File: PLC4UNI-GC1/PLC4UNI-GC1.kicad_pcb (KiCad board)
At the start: 4 copper layers, 102.4 x 83.1 mm, 160 parts, among them J1 Conn_02x07_Odd_Even, K1 G5V-1, K2 G5V-1, Q1 NCE60P04R, Q2 ZXMS6004FFQTA, Q3 ZXMS6004FFQTA, Q4 ZXMS6004FFQTA, Q5 ZXMS6004FFQTA, SW1 TS-1088-AR02016, U1 ESP32-S3-WROOM-1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

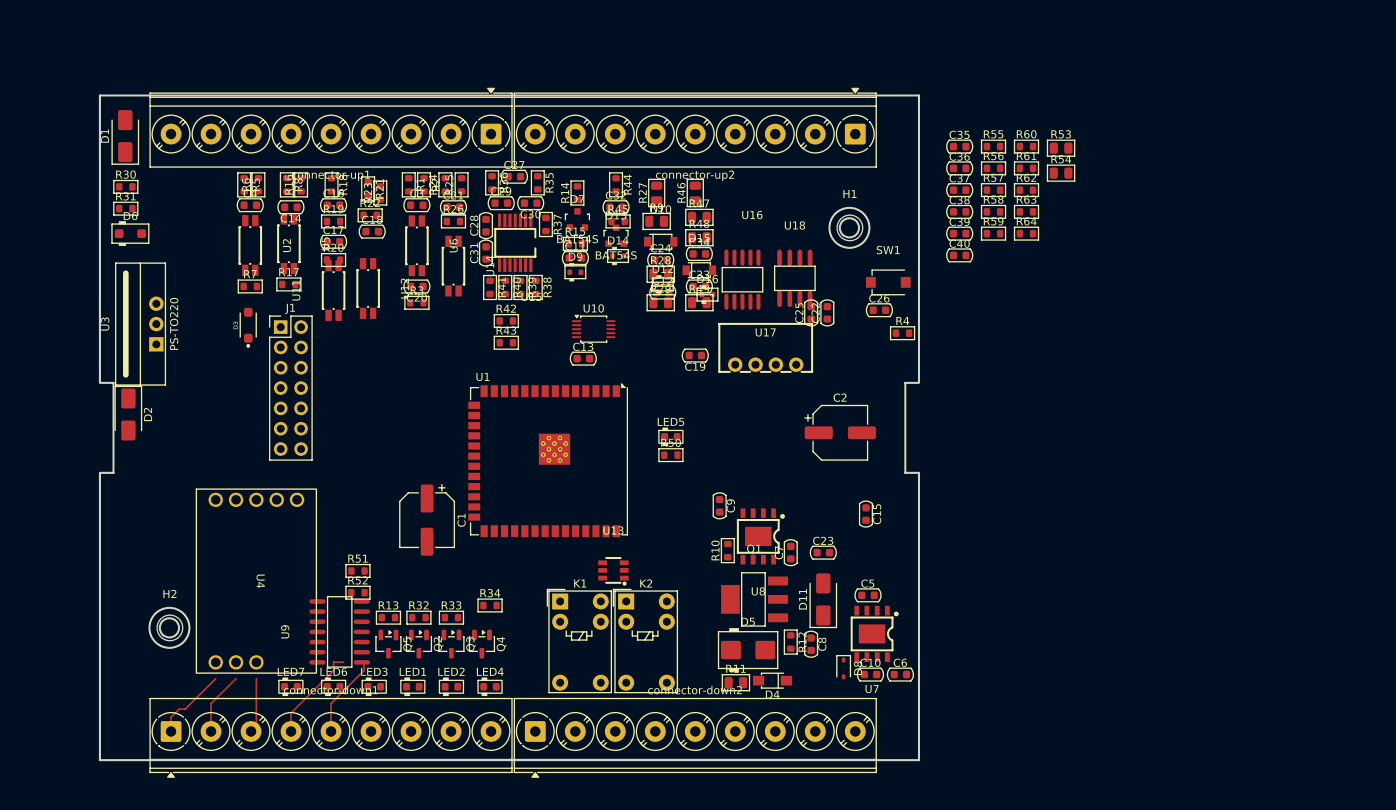
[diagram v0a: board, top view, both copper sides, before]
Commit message: Colocadas el 80% de las piezas
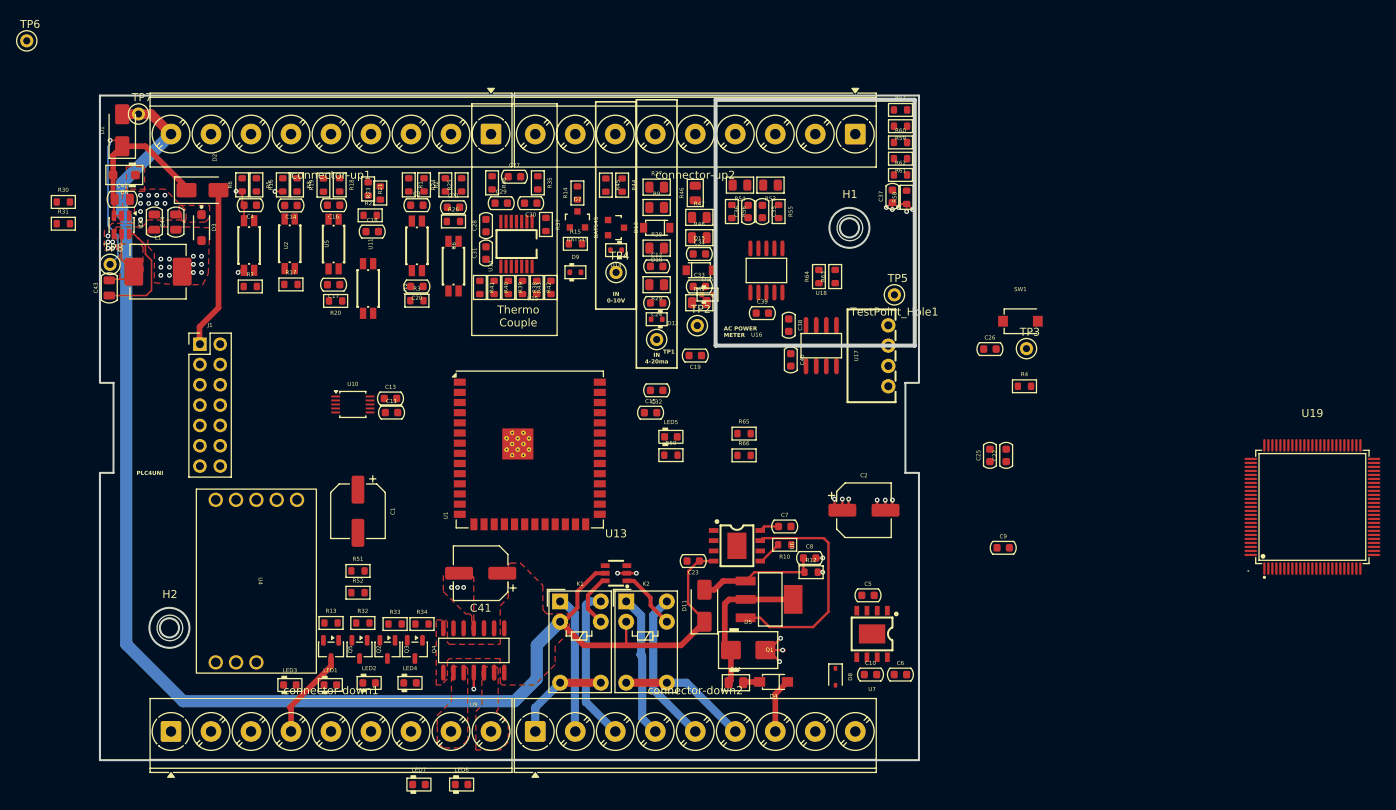
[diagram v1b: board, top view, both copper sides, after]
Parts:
- added C41: 47UF, Capacitor_SMD:CP_Elec_6.3x7.7, F.Cu at (134.6, 120.4)
- added C42: 10uF, Capacitor_SMD_AKL:C_0805_2012Metric, F.Cu at (89.8, 73.7)
- added C43: 100NF, Capacitor_SMD_AKL:C_0805_2012Metric, F.Cu at (88.2, 84.8)
- added C44: 22uF, Capacitor_SMD_AKL:C_0805_2012Metric, F.Cu at (96.5, 76.5)
- added C45: 22uF, Capacitor_SMD_AKL:C_0805_2012Metric, F.Cu at (93.8, 76.5)
- added L1: 10uH, Inductor_SMD:L_APV_APH0630, F.Cu at (94.3, 82.7)
- added R65: 4.7K, Resistor_SMD_AKL:R_0603_1608Metric, F.Cu at (167.5, 103.0)
- added R66: 4.7K, Resistor_SMD_AKL:R_0603_1608Metric, F.Cu at (167.5, 105.7)
- added TP1: TestPoint_Hole1, 4ms_TestPoint:TestPoint_WireHole, F.Cu at (156.6, 91.2)
- added TP2: TestPoint_Hole1, 4ms_TestPoint:TestPoint_WireHole, F.Cu at (161.7, 89.5)
- added TP3: TestPoint_Hole1, 4ms_TestPoint:TestPoint_WireHole, F.Cu at (202.8, 92.4)
- added TP4: TestPoint_Hole1, 4ms_TestPoint:TestPoint_WireHole, F.Cu at (151.5, 82.8)
- added TP5: TestPoint_Hole1, 4ms_TestPoint:TestPoint_WireHole, F.Cu at (186.3, 85.6)
- added TP6: TestPoint_Hole1, 4ms_TestPoint:TestPoint_WireHole, F.Cu at (77.9, 53.9)
- added TP7: TestPoint_Hole1, 4ms_TestPoint:TestPoint_WireHole, F.Cu at (91.8, 63.0)
- added TP8: TestPoint_Hole1, 4ms_TestPoint:TestPoint_WireHole, F.Cu at (88.3, 81.8)
- added U19: LCMXO256C-3TN100C, EasyEDA:TQFP-100_L14.0-W14.0-P0.50-LS16.0-BL, F.Cu at (238.6, 112.1)
- R14, R44: value 3.3K -> 2.2K
- R15, R45: value 2.2K -> 1.05K
- R17, R20, R23, R26, R3, R7: value 10K -> 22K
- U3: value PS-TO220 -> AP63203WU; footprint MG_footprints:PS-TO-220-3_Vertical -> Package_TO_SOT_SMD:TSOT-23-6
- moved R54 40.2 mm to (167.0, 71.9), turned to 180 degrees
- moved R53 36.6 mm to (170.8, 71.9), turned to 180 degrees
- moved C9 35.8 mm to (199.9, 117.3), turned to 0 degrees
- moved R56 33.2 mm to (166.0, 75.2), turned to -90 degrees
- moved U10 31.5 mm to (118.6, 99.3)
- moved C11 30.0 mm to (123.4, 100.3)
- moved C15 29.8 mm to (155.8, 100.4), turned to 0 degrees
- moved D2 29.5 mm to (99.8, 72.5), turned to 0 degrees
- moved C22 28.6 mm to (200.3, 105.7)
- moved C25 28.6 mm to (198.2, 105.7)
- moved R55 28.1 mm to (171.8, 75.2), turned to -90 degrees
- moved C36 27.0 mm to (168.0, 75.2), turned to 90 degrees
- moved C39 26.6 mm to (169.8, 87.9)
- moved R64 26.5 mm to (176.9, 83.3), turned to 90 degrees
- moved C35 26.0 mm to (169.8, 75.2), turned to -90 degrees
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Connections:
- D1 pad 1: Net-(D1-K) -> /PowerSupply/vdc_in
- D2 pad 1: Net-(D1-K) -> /PowerSupply/vdc_in
- D6 pad 2: +24V -> /PowerSupply/vdc_in
- U3 pad 1: Net-(D1-K) -> +3.3V
- U3 pad 2: GND -> /PowerSupply/vdc_in
- U3 pad 3: +3.3V -> /PowerSupply/vdc_in
- connector-down1 pad 4: /control/CON_OUT_PNP1 -> /control/CON_OUT_NPN1
- connector-down1 pad 5: /control/CON_OUT_PNP2 -> /control/CON_OUT_NPN2
- connector-down1 pad 6: /control/CON_OUT_NPN1 -> /control/CON_OUT_NPN3
- connector-down1 pad 7: /control/CON_OUT_NPN2 -> /control/CON_OUT_NPN4
- connector-down1 pad 8: /control/CON_OUT_NPN3 -> /control/CON_OUT_PNP1
- connector-down1 pad 9: /control/CON_OUT_NPN4 -> /control/CON_OUT_PNP2
- connector-down2 pad 4: /control/CON_OUT_RLY2_COM -> /control/CON_OUT_RLY2_NC
- connector-down2 pad 5: /control/CON_OUT_RLY2_NC -> /control/CON_OUT_RLY2_NO
- connector-down2 pad 6: /control/CON_OUT_RLY2_NO -> /control/CON_OUT_RLY2_COM
- connector-up2 pad 1: /control/CON-IN_CT_P -> /control/CON-IN_VAC_P
- connector-up2 pad 2: /control/CON-IN_CT_N -> Earth
- connector-up2 pad 3: /control/CON-IN_VAC_P -> /control/CON-IN_CT_P
- connector-up2 pad 4: /control/CON-IN_VAC_N -> /control/CON-IN_CT_N
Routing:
- net +24V: track 0.00 -> 202.6 mm, vias 0 -> 2
- net /PowerSupply/vdc_in: track 0.00 -> 39.1 mm, vias 0 -> 1
- net Net-(U8-IOUT): track 0.00 -> 29.1 mm
- net +5V: track 0.00 -> 20.5 mm
- net /control/CON_OUT_RLY1_NO: track 0.00 -> 19.4 mm
- net Net-(D5-K): track 0.00 -> 19.3 mm
- net /control/CON_OUT_RLY2_NO: track 0.00 -> 19.1 mm
- net GND: track 0.00 -> 19.1 mm, vias 0 -> 29
- net /control/CON_OUT_RLY2_NC: track 0.00 -> 17.9 mm
- net /control/CON_OUT_RLY1_NC: track 0.00 -> 17.2 mm
- net /control/CON_OUT_RLY2_COM: track 0.00 -> 16.2 mm
- net Net-(D11-A2): track 0.00 -> 15.3 mm
- net Net-(U3-BST): track 0.00 -> 14.1 mm
- net /control/CON_OUT_RLY1_COM: track 0.00 -> 12.5 mm
- net /control/CON_OUT_PNP1: track 12.1 -> 0.00 mm
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- added copper zone on F.Cu, net +24V
- added copper zone on F.Cu, net +3.3V
- added copper zone on In2.Cu, net +3.3V
- added copper zone on F.Cu, net /PowerSupply/sw
- added copper zone on F.Cu, net /control/CON_OUT_PNP1
- added copper zone on F.Cu, net /control/CON_OUT_PNP2
- added copper zone on In1.Cu, net Earth
- added copper zone on F.Cu, net GND
- added copper zone on In1.Cu, net GND
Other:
- outline, holes or cut-outs redrawn
- board text added: "AC POWER METER"
- board text added: "IN 0-10V"
- board text added: "IN 4-20ma"
- board text added: "PLC4UNI"
- board text added: "Thermo Couple"

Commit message: Avances en colocacion de piezas y verificacion de componentes
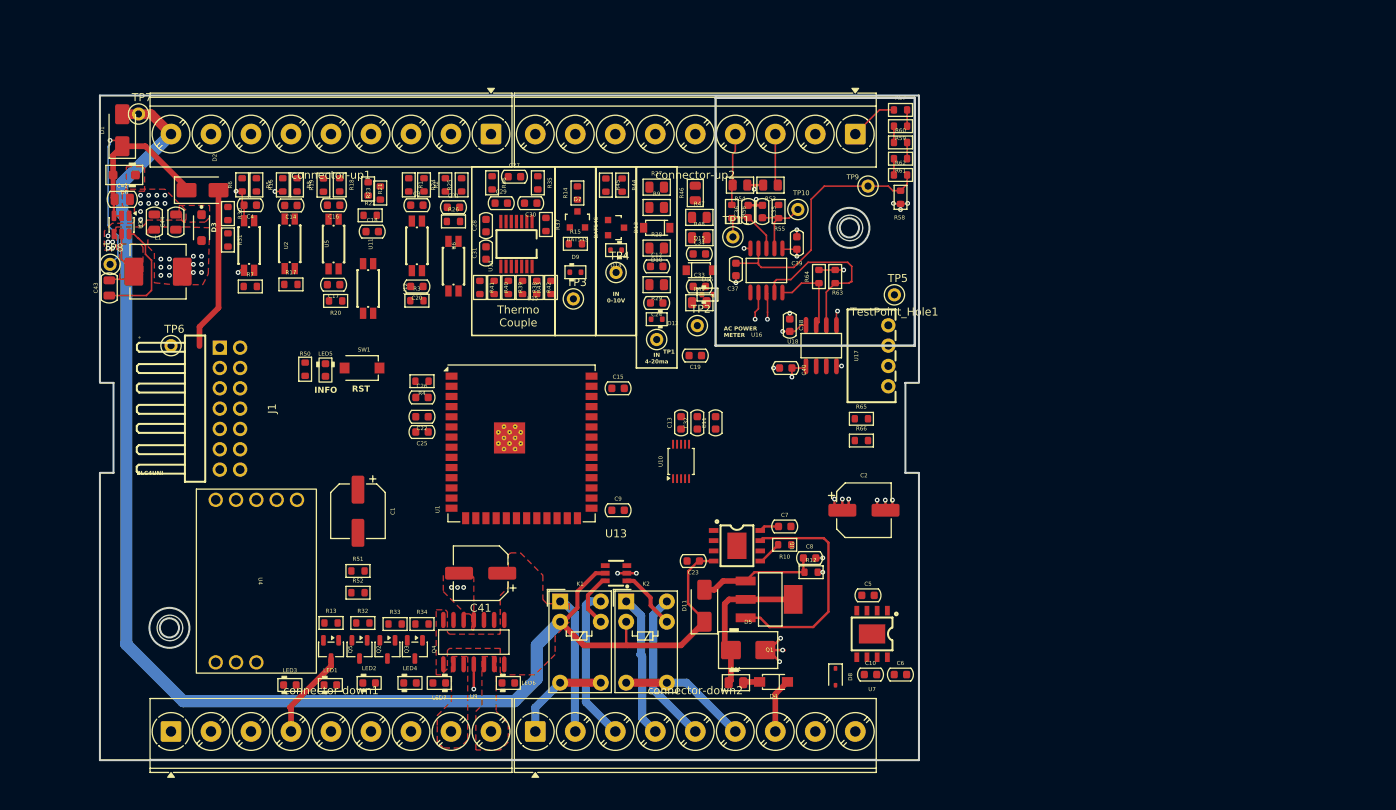
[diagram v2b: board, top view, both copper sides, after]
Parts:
- removed U19: LCMXO256C-3TN100C, EasyEDA:TQFP-100_L14.0-W14.0-P0.50-LS16.0-BL
- added TP10: TestPoint_Hole1, 4ms_TestPoint:TestPoint_WireHole, F.Cu at (174.2, 75.0)
- added TP11: TestPoint_Hole1, 4ms_TestPoint:TestPoint_WireHole, F.Cu at (166.1, 78.4)
- added TP9: TestPoint_Hole1, 4ms_TestPoint:TestPoint_WireHole, F.Cu at (183.0, 72.0)
- J1: value Conn_02x07_Odd_Even -> PZ254R-12-14P; footprint Connector_PinHeader_2.54mm:PinHeader_2x07_P2.54mm_Vertical -> EasyEDA:HDR-TH_14P-P2.54-H-M-R2-C7-S2.54
- moved SW1 82.5 mm to (119.8, 94.8), turned to 180 degrees
- moved R4 75.3 mm to (127.3, 96.4), turned to 180 degrees
- moved C22 73.2 mm to (127.3, 100.9), turned to 180 degrees
- moved C26 71.3 mm to (127.3, 98.5)
- moved C25 71.1 mm to (127.3, 102.8), turned to 180 degrees
- moved TP3 57.0 mm to (146.2, 86.1)
- moved C9 48.4 mm to (151.8, 112.6)
- moved R50 47.0 mm to (112.6, 94.9), turned to 90 degrees
- moved LED5 44.0 mm to (115.2, 95.0), turned to -90 degrees
- moved TP6 42.2 mm to (95.9, 92.0)
- moved U10 41.6 mm to (159.6, 106.5), turned to 90 degrees
- moved C11 40.5 mm to (164.0, 101.6), turned to 90 degrees
- moved C13 36.4 mm to (159.6, 101.6), turned to 90 degrees
- moved C37 21.6 mm to (166.5, 82.5)
- moved R31 20.7 mm to (103.0, 78.8), turned to -90 degrees
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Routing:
- net Net-(U16-VP): track 0.00 -> 33.2 mm
- net Net-(U16-RX/SDI): track 0.00 -> 22.0 mm
- net VCC: track 0.00 -> 12.5 mm, vias 0 -> 4
- net Net-(U16-TX/SDO): track 0.00 -> 10.4 mm
- net Earth: track 9.47 -> 19.6 mm, vias 5 -> 11
- net /control/CON-IN_CT_N: track 0.00 -> 9.49 mm
- net Net-(U16-IN): track 0.00 -> 9.28 mm
- net Net-(U16-IP): track 0.00 -> 9.00 mm
- net /control/CON-IN_CT_P: track 0.00 -> 6.51 mm
- net /control/CON-IN_VAC_P: track 0.00 -> 6.08 mm
- net +3.3V: track 7.08 -> 10.1 mm, vias 16 -> 17
- net Net-(R57-Pad2): track 0.00 -> 2.03 mm
- net Net-(R61-Pad2): track 0.00 -> 2.03 mm
- net Net-(R60-Pad2): track 0.00 -> 2.03 mm
- net Net-(R59-Pad2): track 0.00 -> 2.03 mm
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- added copper zone on In2.Cu, net VCC
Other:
- outline, holes or cut-outs redrawn
- board text added: "INFO"
- board text added: "RST"
